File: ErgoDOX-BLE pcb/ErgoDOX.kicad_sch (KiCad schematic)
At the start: 100 parts, among them J1 Conn_01x04, J2 Conn_01x02_Female, J4 Conn_01x02, J5 Conn_01x02, J6 6PIN, P1 USB_C_Plug_USB2.0, Q1 Q_NPN_BCE, SW0:10 SW0:3, SW0:11 SW0:2, SW0:12 SW0:1, SW0:7 SW0:6, SW0:8 SW0:5, SW0:9 SW0:4, SW1:10 SW1:3, SW1:11 SW1:2, SW1:12 SW1:1, SW1:13 SW1:0, SW1:9 SW1:4, SW2:10 SW2:3, SW2:11 SW2:2, SW2:12 SW2:1, SW2:13 SW2:0, SW2:7 SW2:6, SW2:8 SW2:5, SW2:9 SW2:4, SW3:10 SW3:3, SW3:11 SW3:2, SW3:12 SW3:1, SW3:13 SW3:0, SW3:8 SW3:5, SW3:9 SW3:4, SW4:10 SW4:3, SW4:11 SW4:2, SW4:12 SW4:1, SW4:13 SW4:0, SW4:7 SW4:6, SW4:8 SW4:5, SW4:9 SW4:4, SW5:10 SW5:3, SW5:11 SW5:2, SW5:12 SW5:1, SW5:13 SW5:0, SW5:7 SW5:6, SW5:8 SW5:5, SW5:9 SW5:4, U1 MCP23018

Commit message: Add capacitor
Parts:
- added C2: C, Capacitor_THT:C_Disc_D3.8mm_W2.6mm_P2.50mm, symbol Device:C
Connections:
- net +3V3: now also C2.1
- net GND: now also C2.2
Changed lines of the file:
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@@
   (symbol (lib_name "GND_1") (lib_id "power:GND") (at 193.04 40.64 0) (unit 1)
     (in_bom yes) (on_board yes) (fields_autoplaced)
-    (property "Reference" "#PWR?" (id 0) (at 193.04 46.99 0)
+    (property "Reference" "#PWR030" (id 0) (at 193.04 46.99 0)
       (effects (font (size 1.27 1.27)) hide)
     )
@@
     )
     (property "Datasheet" "~" (id 3) (at 188.595 223.52 0)
+      (effects (font (size 1.27 1.27)) hide)
+    )
+    (pin "1")
+    (pin "2")
+  )
+  (symbol (lib_id "Device:C") (at 198.12 73.66 0) (unit 1)
+    (in_bom yes) (on_board yes) (fields_autoplaced)
+    (property "Reference" "C2" (id 0) (at 201.93 72.3899 0)
+      (effects (font (size 1.27 1.27)) (justify left))
+    )
+    (property "Value" "C" (id 1) (at 201.93 74.9299 0)
+      (effects (font (size 1.27 1.27)) (justify left))
+    )
+    (property "Footprint" "Capacitor_THT:C_Disc_D3.8mm_W2.6mm_P2.50mm" (id 2) (at 199.0852 77.47 0)
+      (effects (font (size 1.27 1.27)) hide)
+    )
+    (property "Datasheet" "~" (id 3) (at 198.12 73.66 0)
       (effects (font (size 1.27 1.27)) hide)
     )
@@
     (pin "2")
   )
+  (symbol (lib_id "power:+3V3") (at 198.12 69.85 0) (unit 1)
+    (in_bom yes) (on_board yes) (fields_autoplaced)
+    (property "Reference" "#PWR033" (id 0) (at 198.12 73.66 0)
+      (effects (font (size 1.27 1.27)) hide)
+    )
+    (property "Value" "+3V3" (id 1) (at 198.12 66.2455 0))
+    (property "Footprint" "" (id 2) (at 198.12 69.85 0)
+      (effects (font (size 1.27 1.27)) hide)
+    )
+    (property "Datasheet" "" (id 3) (at 198.12 69.85 0)
+      (effects (font (size 1.27 1.27)) hide)
+    )
+    (pin "1")
+  )
   (symbol (lib_id "Connector_Generic:Conn_01x04") (at 204.47 139.7 0) (unit 1)
     (in_bom yes) (on_board yes) (fields_autoplaced)
@@
     (pin "3")
     (pin "4")
+  )
+  (symbol (lib_id "component:GND") (at 196.85 77.47 270) (unit 1)
+    (in_bom yes) (on_board yes)
+    (property "Reference" "#PWR031" (id 0) (at 196.85 77.47 0)
+      (effects (font (size 0.762 0.762)) hide)
+    )
+    (property "Value" "GND" (id 1) (at 195.072 77.47 0)
+      (effects (font (size 0.762 0.762)) hide)
+    )
+    (property "Footprint" "" (id 2) (at 196.85 77.47 0)
+      (effects (font (size 1.524 1.524)) hide)
+    )
+    (property "Datasheet" "" (id 3) (at 196.85 77.47 0)
+      (effects (font (size 1.524 1.524)) hide)
+    )
+    (pin "1")
   )
   (symbol (lib_id "power:+3V3") (at 318.135 22.86 270) (unit 1)
@@
       (reference "#PWR029") (unit 1) (value "+3V3") (footprint "")
     )
+    (path "/7dfa7247-12a0-4888-9d03-1bdfdd878cd3"
+      (reference "#PWR030") (unit 1) (value "GND") (footprint "")
+    )
+    (path "/d9165053-61d3-4304-89c2-abdc1efcb115"
+      (reference "#PWR031") (unit 1) (value "GND") (footprint "")
+    )
     (path "/843b7e0c-6712-4881-9be2-1926b0335f1a"
       (reference "#PWR032") (unit 1) (value "GND") (footprint "")
     )
+    (path "/d0bac614-5965-45ae-9619-14212e3ab5b6"
+      (reference "#PWR033") (unit 1) (value "+3V3") (footprint "")
+    )
     (path "/3776ed17-29da-4dcb-90b3-a7606449a11d"
       (reference "#PWR0101") (unit 1) (value "GND") (footprint "")
@@
       (reference "#PWR0107") (unit 1) (value "+5V") (footprint "")
     )
-    (path "/7dfa7247-12a0-4888-9d03-1bdfdd878cd3"
-      (reference "#PWR?") (unit 1) (value "GND") (footprint "")
-    )
     (path "/dc3e5149-0691-4e48-82aa-18a33c58d220"
       (reference "A1") (unit 1) (value "Adafruit_Feather_32u4_BluefruitLE") (footprint "Module:Adafruit_Feather")
@@
       (reference "C1") (unit 1) (value "C") (footprint "Capacitor_THT:CP_Radial_Tantal_D5.0mm_P5.00mm")
     )
+    (path "/a0eea18c-fd7a-428a-808b-290b4bd06294"
+      (reference "C2") (unit 1) (value "C") (footprint "Capacitor_THT:C_Disc_D3.8mm_W2.6mm_P2.50mm")
+    )
     (path "/0a4aac90-e59d-4cda-b0a5-9767da3bc5a3"

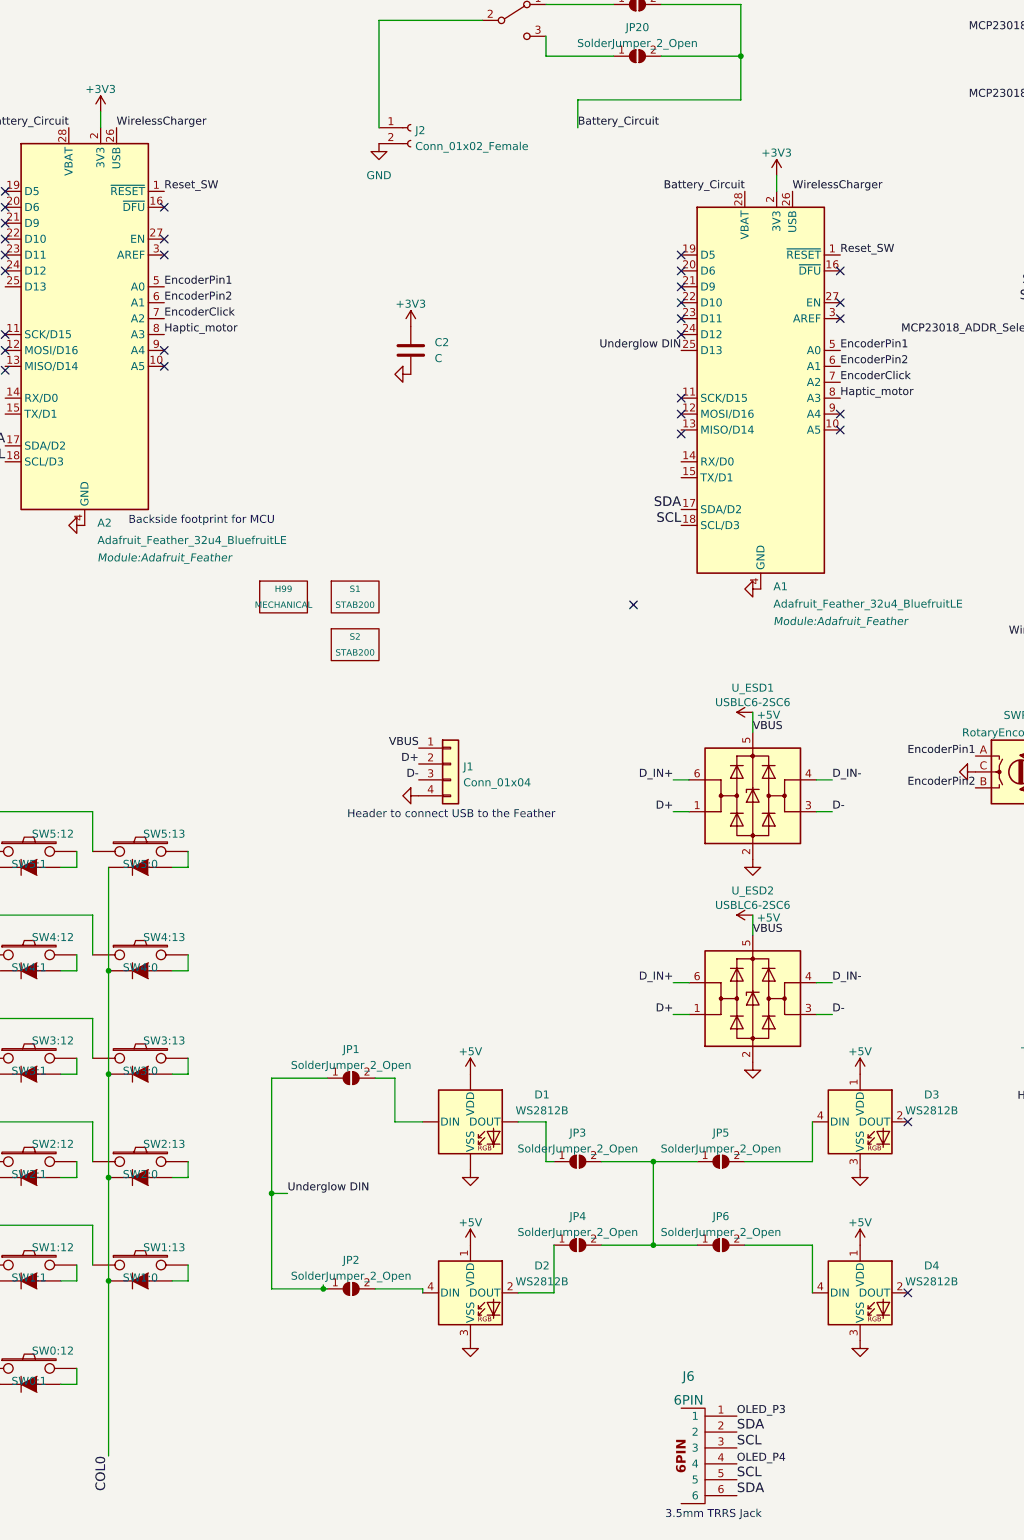
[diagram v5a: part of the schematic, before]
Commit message: Add jumpers to fix TRRS
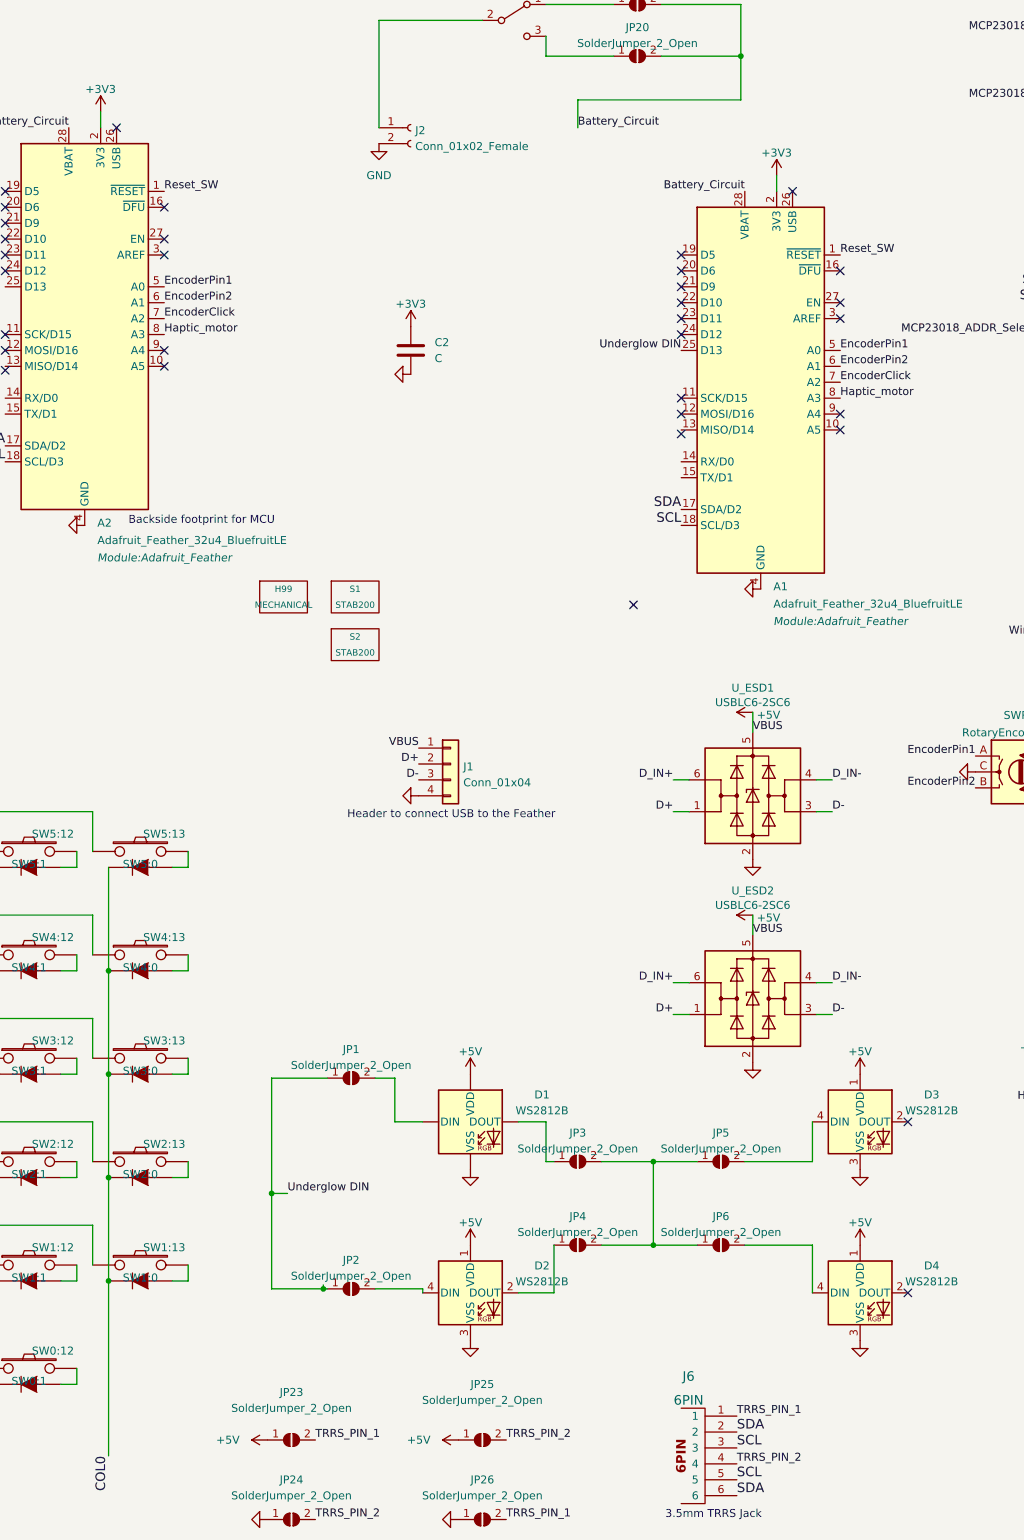
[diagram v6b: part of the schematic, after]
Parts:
- added JP23, JP24, JP25, JP26: SolderJumper_2_Open, Jumper:SolderJumper-2_P1.3mm_Open_RoundedPad1.0x1.5mm, symbol Jumper:SolderJumper_2_Open
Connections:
- net +5V: now also JP23.1 (A), JP25.1 (A)
- net GND: now also JP24.1 (A), JP26.1 (A)
- net OLED_P3: no longer J6.1
- net OLED_P4: no longer J6.4
- net WirelessCharger: no longer A1.26 (USB), A2.26 (USB)
- new net TRRS_PIN_1: J6.1, JP23.2 (B), JP26.2 (B)
- new net TRRS_PIN_2: J6.4, JP24.2 (B), JP25.2 (B)
- no-connect marks 36 -> 38

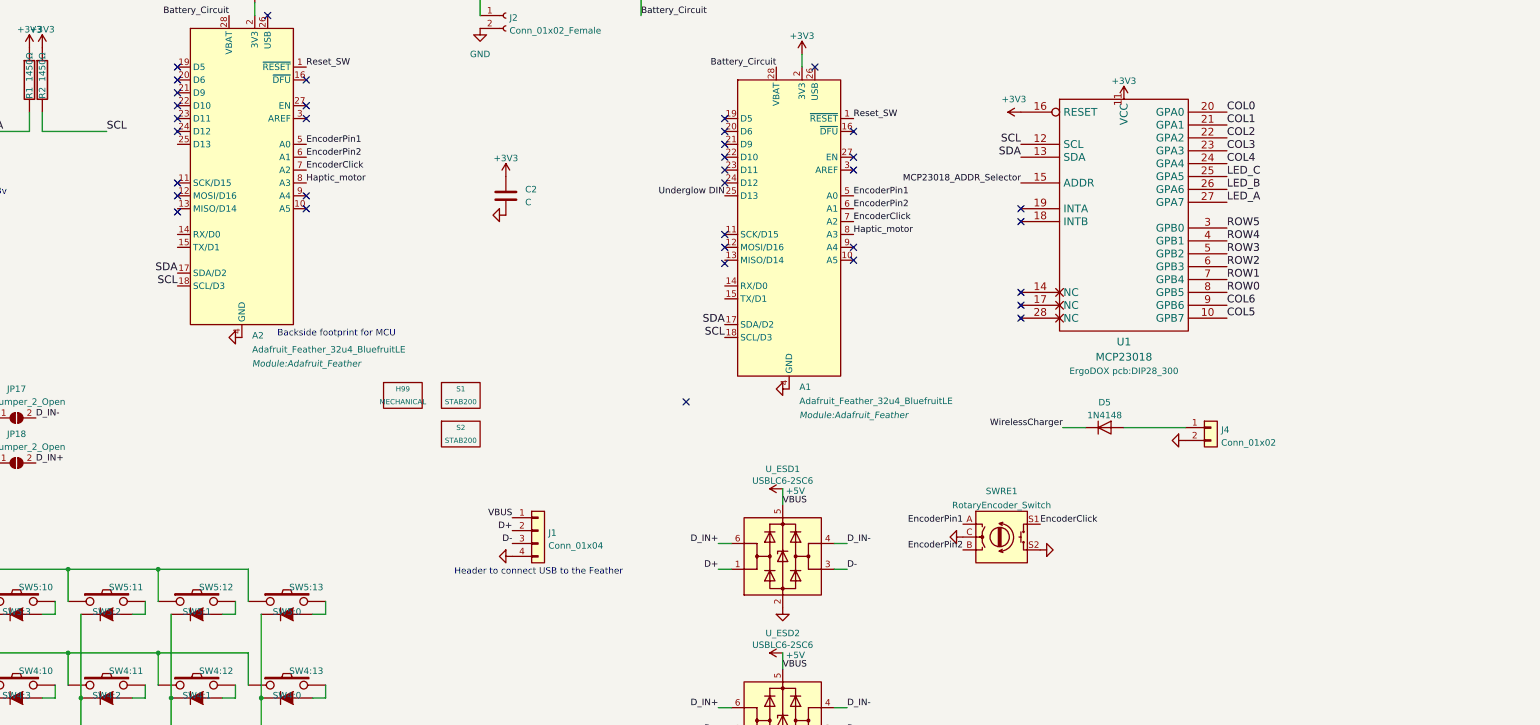
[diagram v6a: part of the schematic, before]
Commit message: Build out charging circuit
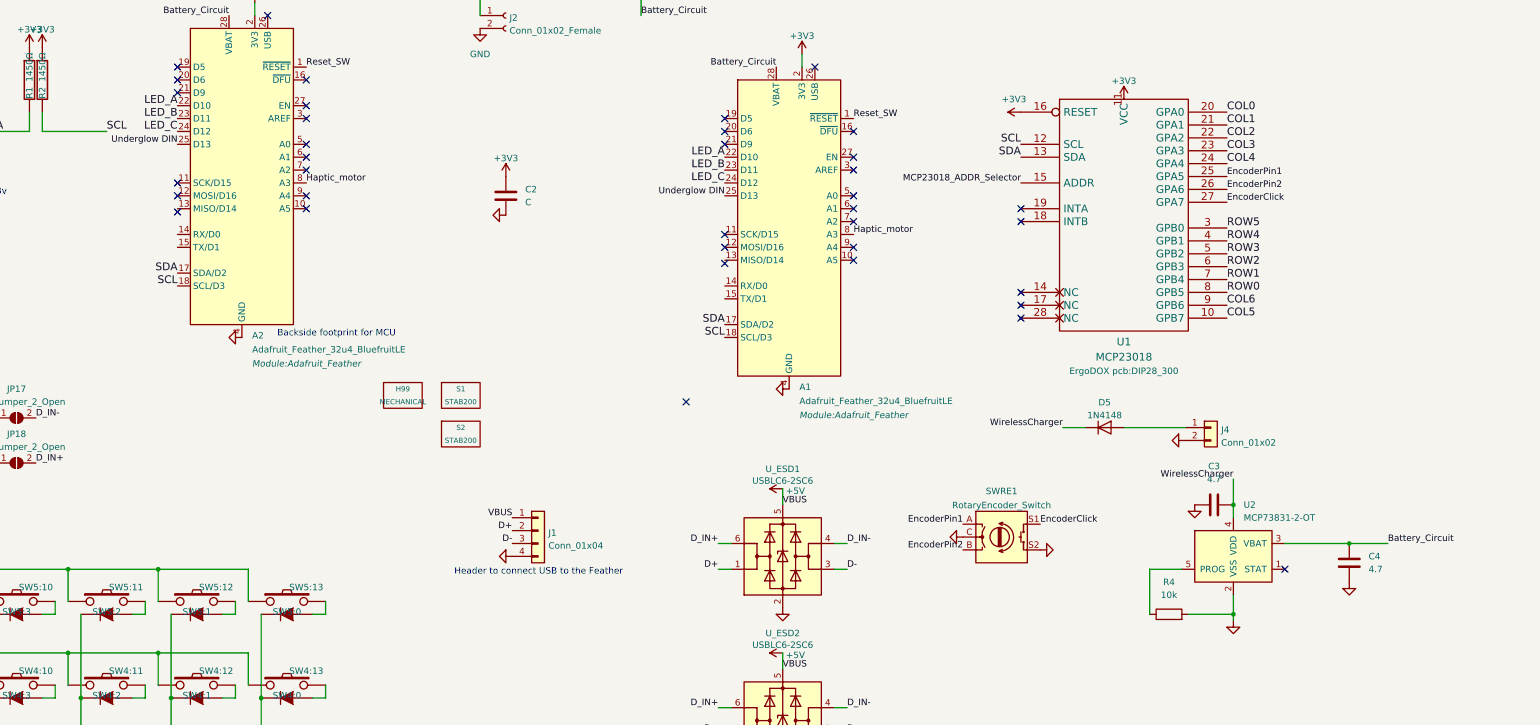
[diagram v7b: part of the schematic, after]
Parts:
- added C3, C4: 4.7, symbol Device:C
- added R4: 10k, symbol Device:R
- added U2: MCP73831-2-OT, Package_TO_SOT_SMD:SOT-23-5, symbol Battery_Management:MCP73831-2-OT
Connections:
- net Battery_Circuit: now also C4.1, U2.3 (VBAT)
- net EncoderClick: now also U1.27 (GPA7); no longer A1.7 (A2), A2.7 (A2)
- net EncoderPin1: now also U1.25 (GPA5); no longer A1.5 (A0), A2.5 (A0)
- net EncoderPin2: now also U1.26 (GPA6); no longer A1.6 (A1), A2.6 (A1)
- net GND: now also C3.2, C4.2, R4.2, U2.2 (VSS)
- net LED_A: now also A1.22 (D10), A2.22 (D10); no longer U1.27 (GPA7)
- net LED_B: now also A1.23 (D11), A2.23 (D11); no longer U1.26 (GPA6)
- net LED_C: now also A1.24 (D12), A2.24 (D12); no longer U1.25 (GPA5)
- net Underglow DIN: now also A2.25 (D13)
- net WirelessCharger: now also C3.1, U2.4 (VDD)
- new net: R4.1, U2.5 (PROG)
- no-connect marks 38 -> 39
